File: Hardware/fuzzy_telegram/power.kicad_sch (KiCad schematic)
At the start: 3 parts, among them U1 STM32MP157DAB1

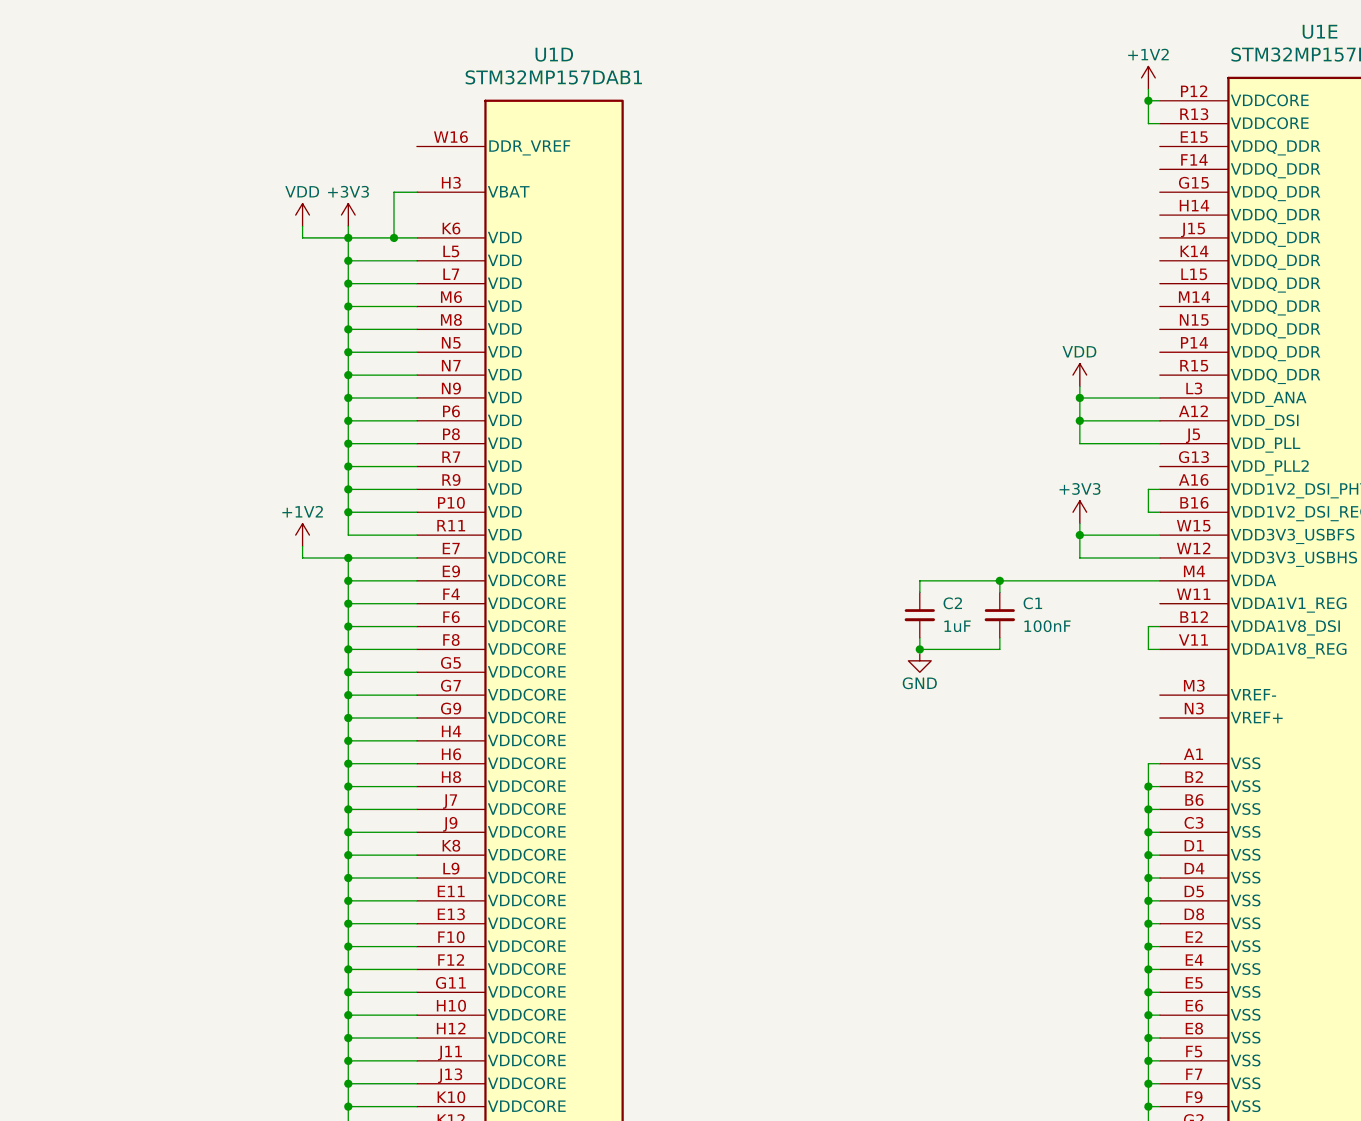
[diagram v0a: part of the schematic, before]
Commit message: STM32MP decoupling caps
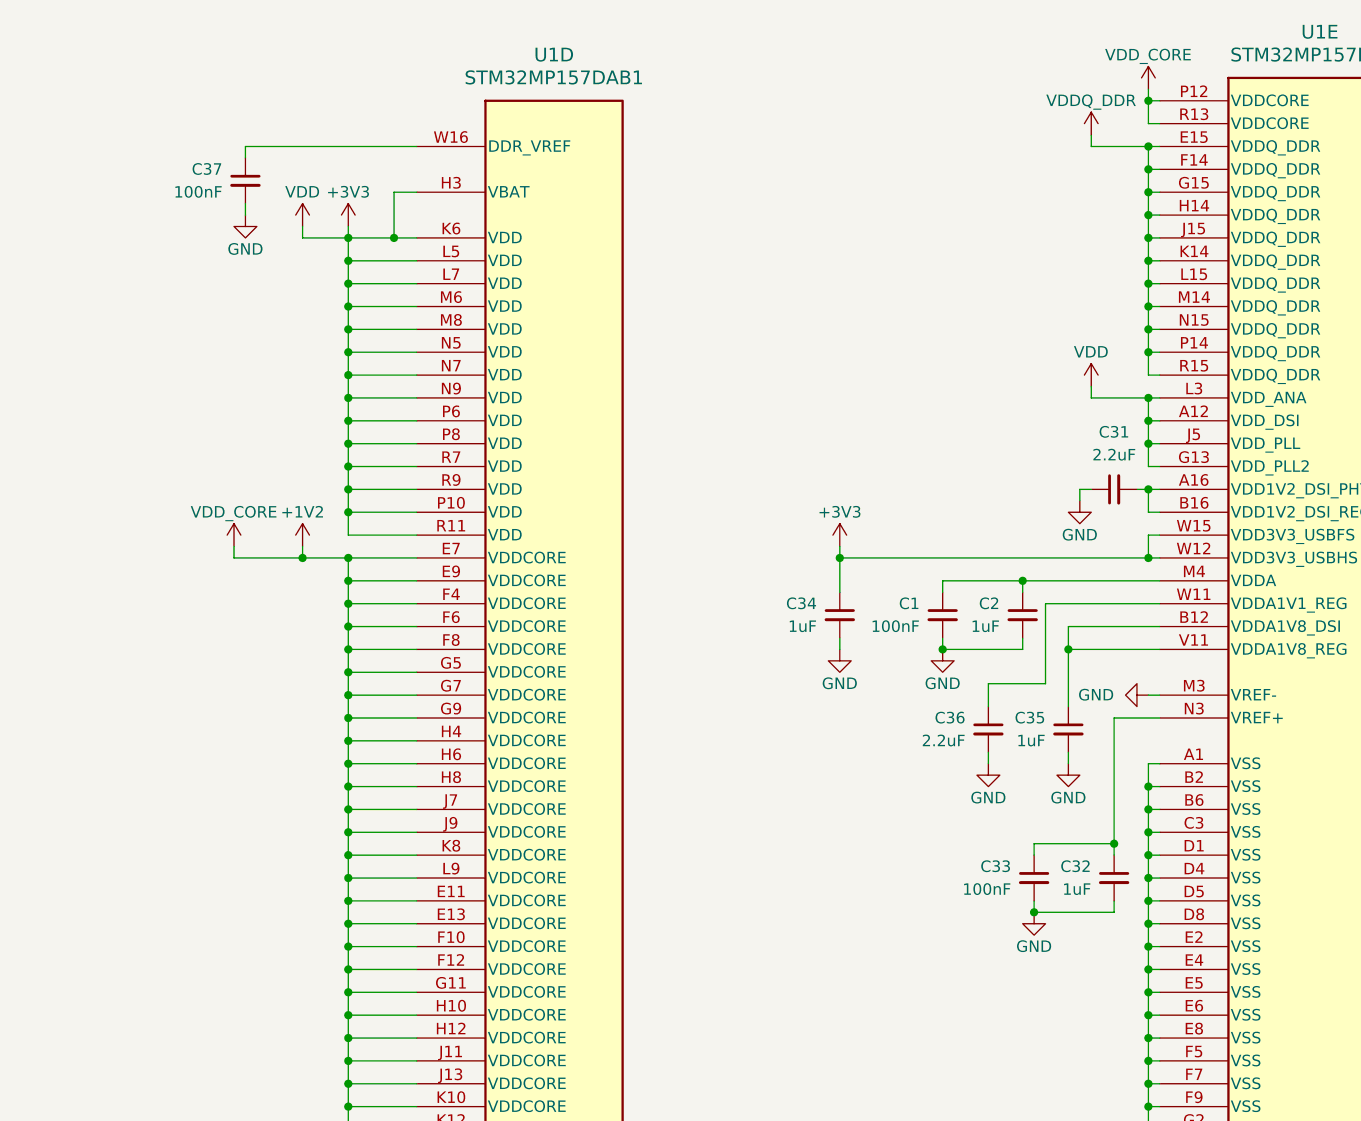
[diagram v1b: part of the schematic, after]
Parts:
- added C31, C36: 2.2uF, symbol Device:C_Small
- added C32, C34, C35: 1uF, symbol Device:C_Small
- added C33, C37: 100nF, symbol Device:C_Small
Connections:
- net +3V3: now also U1.G13 (VDD_PLL2), C34.1
- net GND: now also U1.M3 (VREF-), C31.1, C32.2, C33.2, C34.2, C35.2, C36.2, C37.2
- net at U1.A16 (VDD1V2_DSI_PHY), U1.B16 (VDD1V2_DSI_REG): now also C31.2
- net at U1.B12 (VDDA1V8_DSI), U1.V11 (VDDA1V8_REG): now also C35.1
- net VDDQ_DDR: now reaches U1.E15 (VDDQ_DDR)
- net VDDQ_DDR: now also U1.F14 (VDDQ_DDR), U1.G15 (VDDQ_DDR), U1.H14 (VDDQ_DDR), U1.J15 (VDDQ_DDR), U1.K14 (VDDQ_DDR), U1.L15 (VDDQ_DDR), U1.M14 (VDDQ_DDR), U1.N15 (VDDQ_DDR), U1.P14 (VDDQ_DDR), U1.R15 (VDDQ_DDR)
- net at U1.N3 (VREF+): now also C32.1, C33.1
- net at U1.W11 (VDDA1V1_REG): now also C36.1
- net at U1.W16 (DDR_VREF): now also C37.1
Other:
- moved on the sheet: C1, C2

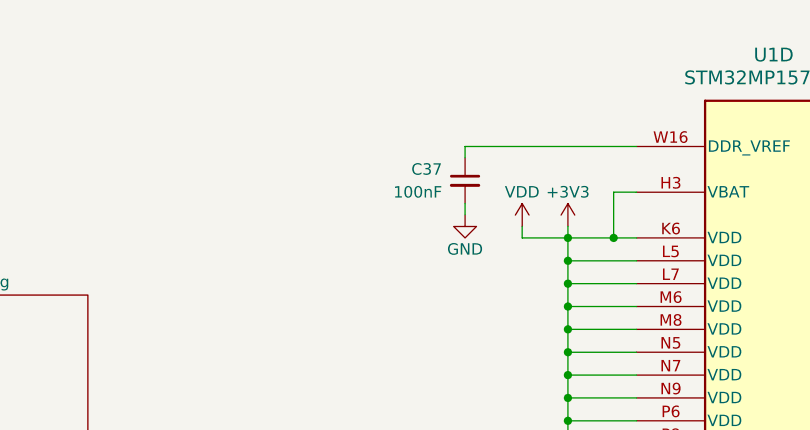
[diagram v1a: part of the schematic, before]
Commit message: add SD card and more
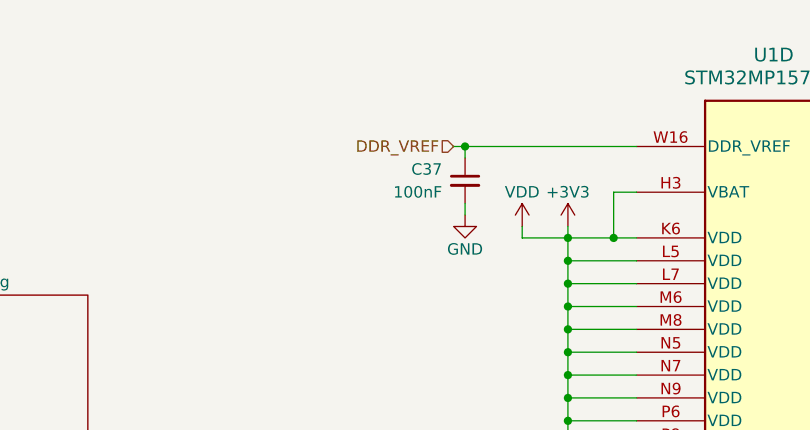
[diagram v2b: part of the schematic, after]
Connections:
- net DDR_VREF: now reaches C37.1, U1.W16 (DDR_VREF)
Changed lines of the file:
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@@
 	)
 	(junction
+		(at 90.17 31.75)
+		(diameter 0)
+		(color 0 0 0 0)
+	)
+	(junction
 		(at 101.6 80.01)
 		(diameter 0)
@@
 	(wire
 		(pts
+			(xy 88.9 31.75) (xy 90.17 31.75)
+		)
+		(stroke
+			(width 0)
+			(type default)
+		)
+	)
+	(wire
+		(pts
 			(xy 255.27 74.93) (xy 255.27 77.47)
 		)
@@
 		)
 	)
+	(hierarchical_label "DDR_VREF"
+		(shape input)
+		(at 88.9 31.75 180)
+		(effects
+			(font
+				(size 1.27 1.27)
+			)
+			(justify right)
+		)
+	)

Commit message: Started power design
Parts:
- added C43, C45, C52, C53, C54, C55: 100nF, symbol Device:C_Small
- added C46, C47, C49, C50, C56, C57: 47uF, symbol Device:C_Small
- added C48, C51, C58: 1uF, symbol Device:C_Small
- added R13, R20: 10k, symbol Device:R_Small
- added R14: 23.2, symbol Device:R_Small
- added R17: 332k, symbol Device:R_Small
- added R18: 100k, symbol Device:R_Small
- added R19: 2k, symbol Device:R_Small
- added R23: 3.5k, symbol Device:R_Small
- added R24: ??, symbol Device:R_Small
- added U5, U6, U7: TPSM33625FRDNR, fuzzy_telegram:RDN0011A-MFG-NO-VIA, symbol fuzzy_telegram:TPSM33625
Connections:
- net +1V2: now also C46.1, C47.1, R19.1, U6.4 (VOUT)
- net +3V3: now also C49.1, C50.1, R14.1, U5.4 (VOUT)
- net GND: now also C43.2, C45.2, C46.2, C47.2, C48.2, C49.2, C50.2, C51.2, C52.2, C53.2, C54.2, C55.2, C56.2, C57.2, C58.2, R13.2, R18.2, R20.2, R24.2, U5.10 (GND), U5.11 (MODE), U6.10 (GND), U6.11 (MODE), U7.10 (GND), U7.11 (MODE)
- net VDDQ_DDR renamed +1V35
- net +1V35: now also C56.1, C57.1, R23.1, U7.4 (VOUT)
- new net: C48.1, U6.8 (VCC)
- new net: C43.1, C45.1, U6.3 (VIN)
- new net: C52.1, C53.1, R17.1, U5.3 (VIN)
- new net: R17.2, R18.1, U5.2 (EN)
- new net: C51.1, U5.8 (VCC)
- new net: R13.1, R14.2, U5.9 (FB)
- new net: R19.2, R20.1, U6.9 (FB)
- new net: R23.2, R24.1, U7.9 (FB)
- new net: C54.1, C55.1, U7.3 (VIN)
- new net: C58.1, U7.8 (VCC)
- new net 1V2_EN: U6.2 (EN)
- new net 1V35_EN: U7.2 (EN)
- no-connect marks 0 -> 3
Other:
- moved on the sheet: C37, U1D
